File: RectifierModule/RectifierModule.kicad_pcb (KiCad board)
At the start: 2 copper layers, 45 x 70 mm, 26 parts, among them J201 RectifierIn, J202 Switch, J203 Digital VA measure, J204 VOut, J301 AC_IN, J302 Rectifier_out, J401 VA, J402 FAN, J403 Extra, Q201 BD139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

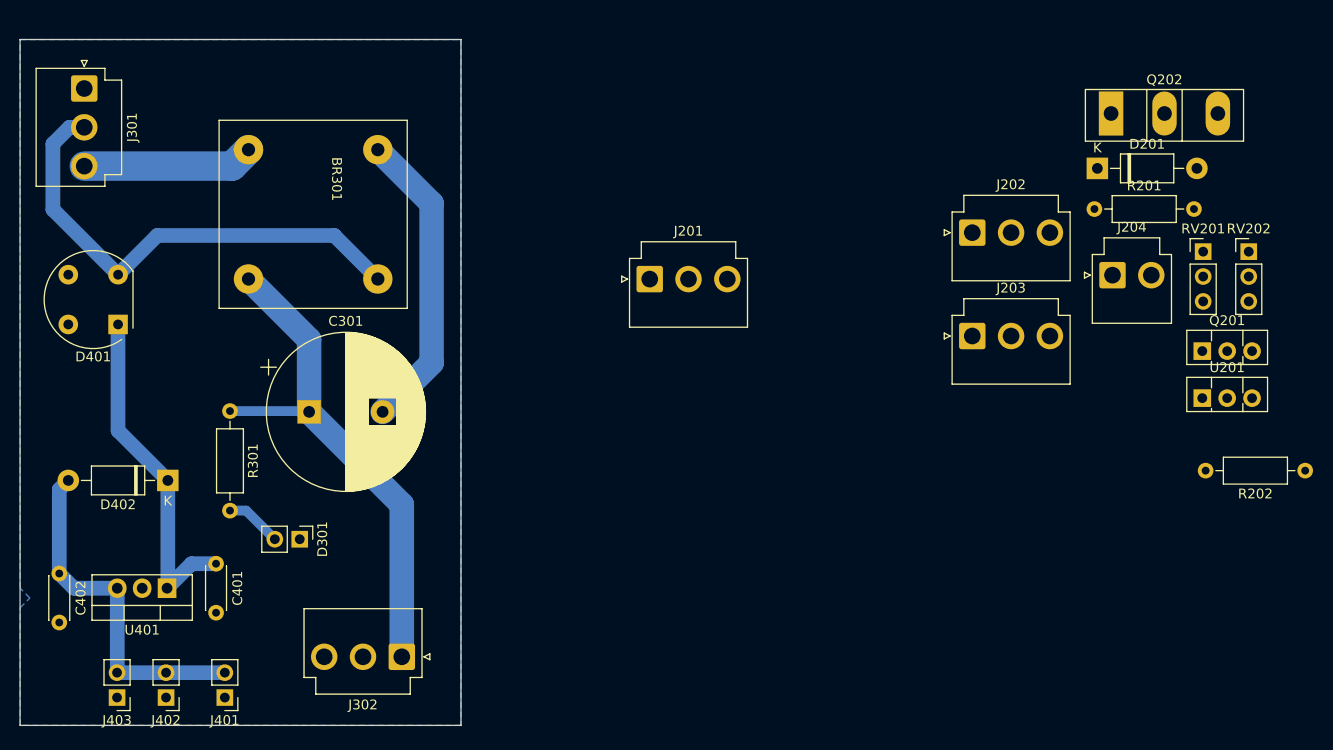
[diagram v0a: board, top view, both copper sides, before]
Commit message: Generated PCB layout
Some minor updates in the schematic and created the PCB layout for the rectifier module
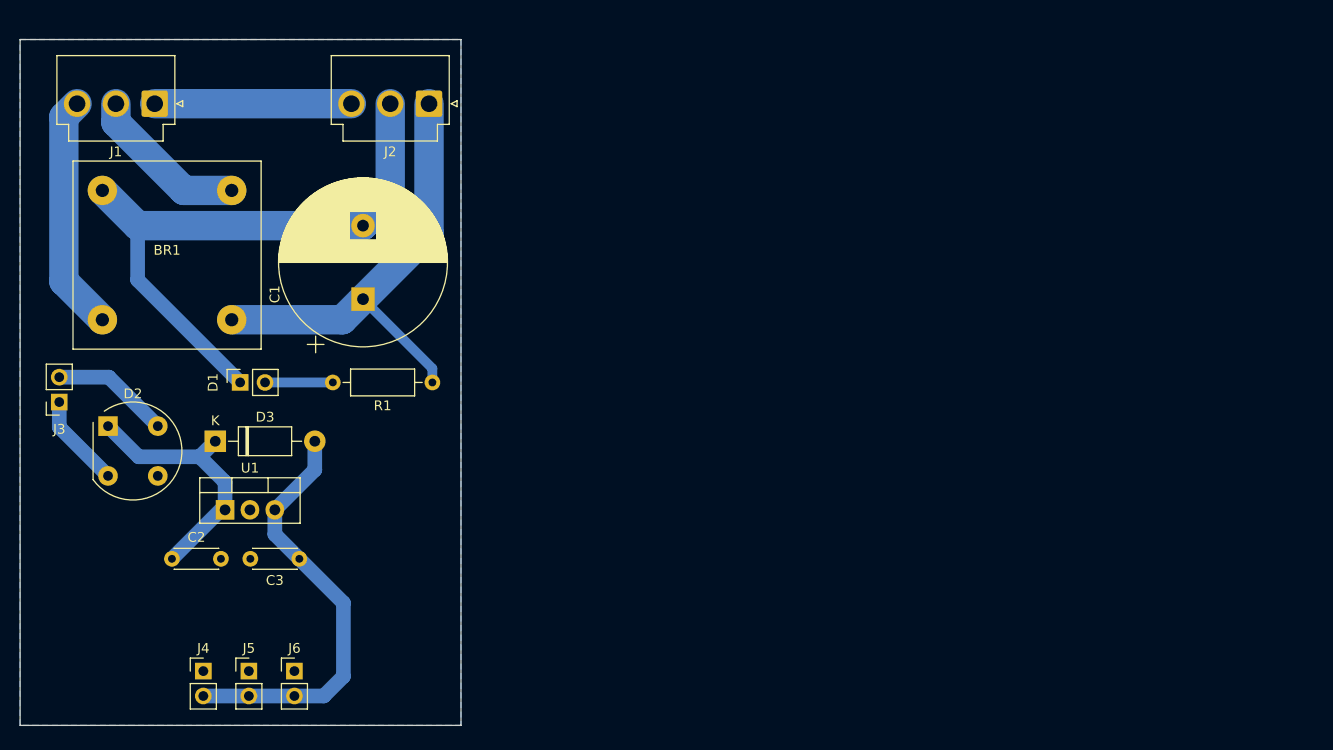
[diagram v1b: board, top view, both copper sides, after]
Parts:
- removed BR301: BRIDGE_RECTIFIER_CLASSIC, BridgeRectifiers:BR-10X
- removed C301: 4700u, Capacitor_THT:CP_Radial_D16.0mm_P7.50mm
- removed C401, C402: .1uF, Capacitor_THT:C_Disc_D4.3mm_W1.9mm_P5.00mm
- removed D201, D402: 1N4007, Diode_THT:D_DO-41_SOD81_P10.16mm_Horizontal
- removed D301: LED, Connector_PinHeader_2.54mm:PinHeader_1x02_P2.54mm_Vertical
- removed D401: W06G, Diode_THT:Diode_Bridge_Round_D9.8mm
- removed J201: RectifierIn, Connector_JST:JST_VH_B3P-VH-B_1x03_P3.96mm_Vertical
- removed J202: Switch, Connector_JST:JST_VH_B3P-VH-B_1x03_P3.96mm_Vertical
- removed J203: Digital VA measure, Connector_JST:JST_VH_B3P-VH_1x03_P3.96mm_Vertical
- removed J204: VOut, Connector_JST:JST_VH_B2P-VH_1x02_P3.96mm_Vertical
- removed J301: AC_IN, Connector_JST:JST_VH_B3P-VH-B_1x03_P3.96mm_Vertical
- removed J302: Rectifier_out, Connector_JST:JST_VH_B3P-VH-B_1x03_P3.96mm_Vertical
- removed J401: VA, Connector_PinHeader_2.54mm:PinHeader_1x02_P2.54mm_Vertical
- removed J402: FAN, Connector_PinHeader_2.54mm:PinHeader_1x02_P2.54mm_Vertical
- removed J403: Extra, Connector_PinHeader_2.54mm:PinHeader_1x02_P2.54mm_Vertical
- removed Q201: BD139, Package_TO_SOT_THT:TO-126-3_Vertical
- removed Q202: TIP2955G, Package_TO_SOT_THT:TO-247-3_Vertical
- removed R201, R202: 220, Resistor_THT:R_Axial_DIN0207_L6.3mm_D2.5mm_P10.16mm_Horizontal
- removed R301: 10k, Resistor_THT:R_Axial_DIN0207_L6.3mm_D2.5mm_P10.16mm_Horizontal
- removed RV201: 5k, Connector_PinHeader_2.54mm:PinHeader_1x03_P2.54mm_Vertical
- removed RV202: 10k, Connector_PinHeader_2.54mm:PinHeader_1x03_P2.54mm_Vertical
- removed U201: LM317, Package_TO_SOT_THT:TO-126-3_Vertical
- removed U401: LM7812_TO220, Package_TO_SOT_THT:TO-220-3_Vertical
- added BR1: BRIDGE_RECTIFIER_CLASSIC, BridgeRectifiers:BR-10X, F.Cu at (31.0, 36.0)
- added C1: 4700u, Capacitor_THT:CP_Radial_D17.0mm_P7.50mm, F.Cu at (51.0, 40.5)
- added C2: .1uF, Capacitor_THT:C_Disc_D4.3mm_W1.9mm_P5.00mm, F.Cu at (31.5, 67.0)
- added C3: .1uF, Capacitor_THT:C_Disc_D4.3mm_W1.9mm_P5.00mm, F.Cu at (44.5, 67.0)
- added D1: LED, Connector_PinSocket_2.54mm:PinSocket_1x02_P2.54mm_Vertical, F.Cu at (38.5, 49.0)
- added D2: W06G, Diode_THT:Diode_Bridge_Round_D9.8mm, F.Cu at (25.0, 53.5)
- added D3: 1N4007, Diode_THT:D_DO-41_SOD81_P10.16mm_Horizontal, F.Cu at (35.9, 55.0)
- added J1: TransformerIn, Connector_JST:JST_VH_B3P-VH-B_1x03_P3.96mm_Vertical, F.Cu at (29.7, 20.6)
- added J2: Rectified Out, Connector_JST:JST_VH_B3P-VH-B_1x03_P3.96mm_Vertical, F.Cu at (57.7, 20.6)
- added J3: AuxIn, Connector_PinSocket_2.54mm:PinSocket_1x02_P2.54mm_Vertical, F.Cu at (20.0, 51.0)
- added J4: VA, Connector_PinHeader_2.54mm:PinHeader_1x02_P2.54mm_Vertical, F.Cu at (34.7, 78.5)
- added J5: FAN, Connector_PinHeader_2.54mm:PinHeader_1x02_P2.54mm_Vertical, F.Cu at (39.4, 78.5)
- added J6: Extra, Connector_PinHeader_2.54mm:PinHeader_1x02_P2.54mm_Vertical, F.Cu at (44.0, 78.5)
- added R1: 220, Resistor_THT:R_Axial_DIN0207_L6.3mm_D2.5mm_P10.16mm_Horizontal, F.Cu at (58.1, 49.0)
- added U1: LM7812_TO220, Package_TO_SOT_THT:TO-220-3_Vertical, F.Cu at (36.9, 62.0)
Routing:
- net /30V-: track 0.00 -> 62.0 mm
- net /LM317_Module/RectifiedOut+: track 53.2 -> 0.00 mm
- net /Auxilliaries/Aux_input_N: track 50.0 -> 0.00 mm
- net /30V+: track 0.00 -> 48.4 mm
- net /Aux_out: track 0.00 -> 43.7 mm
- net /Auxilliaries/Aux_out: track 36.1 -> 0.00 mm
- net /Auxilliaries/RectifiedOut+: track 35.1 -> 0.00 mm
- net /LM317_Module/RectifiedOut-: track 31.1 -> 0.00 mm
- net /12V+: track 0.00 -> 26.9 mm
- net /AC_IN_L: track 0.00 -> 24.2 mm
- net /CentreTap: track 0.00 -> 20.1 mm
- net /Rectifier Module/AC_L: track 17.5 -> 0.00 mm
- net /AC_IN_N: track 0.00 -> 16.6 mm
- net /Aux_input_L: track 0.00 -> 12.1 mm
- net /Aux_input_N: track 0.00 -> 9.60 mm
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
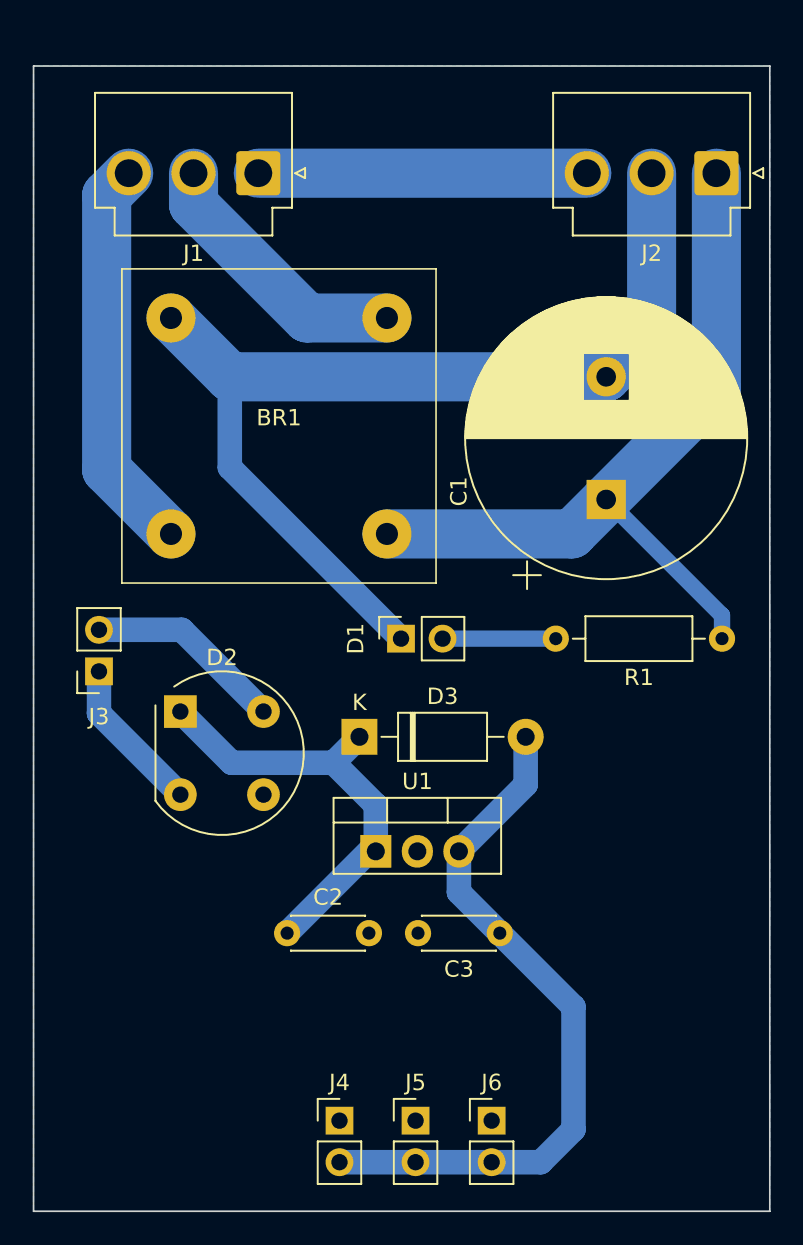
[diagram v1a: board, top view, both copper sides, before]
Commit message: Updated the capacitor at input of 7812
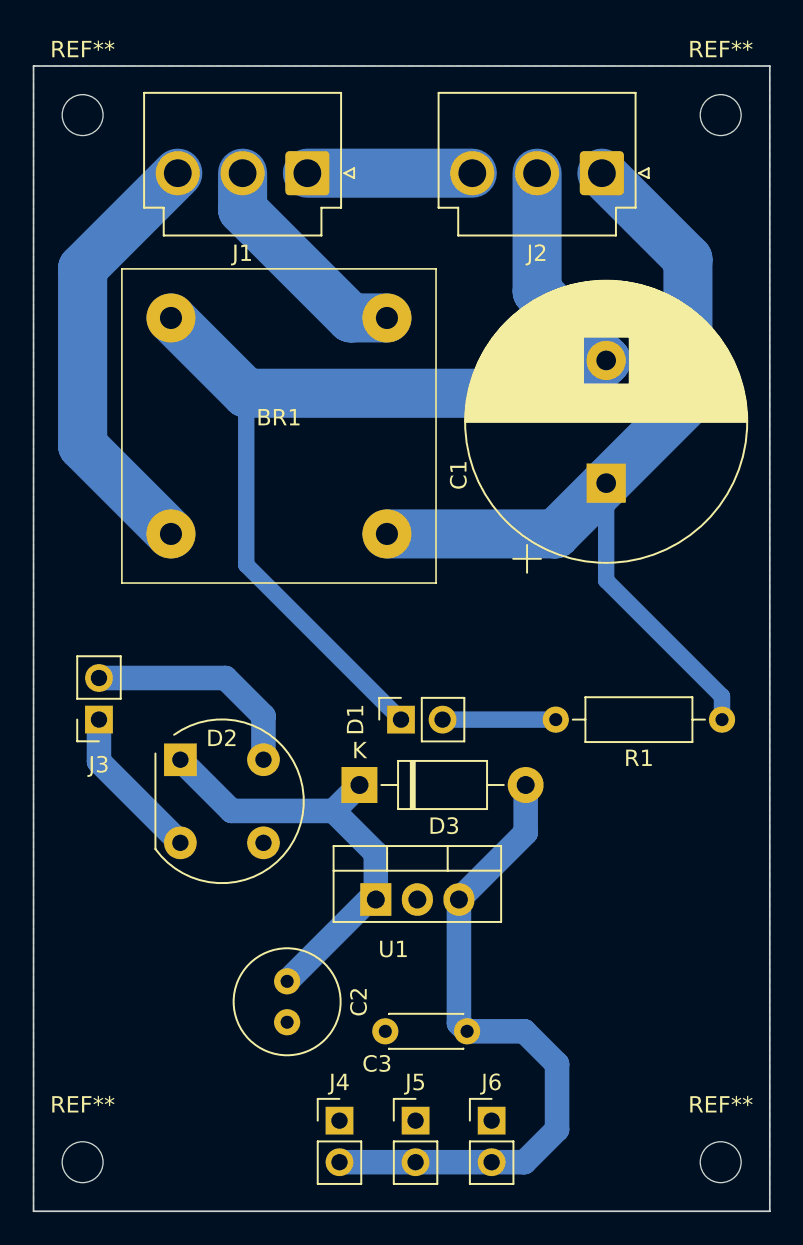
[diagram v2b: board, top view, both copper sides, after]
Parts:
- added REF**: MountingHole_2.5mm, MountingHole:MountingHole_2.5mm, F.Cu at (58.0, 81.0)
- added REF**: MountingHole_2.5mm, MountingHole:MountingHole_2.5mm, F.Cu at (58.0, 17.0)
- added REF**: MountingHole_2.5mm, MountingHole:MountingHole_2.5mm, F.Cu at (19.0, 81.0)
- added REF**: MountingHole_2.5mm, MountingHole:MountingHole_2.5mm, F.Cu at (19.0, 17.0)
- C2: value .1uF -> 100u; footprint Capacitor_THT:C_Disc_D4.3mm_W1.9mm_P5.00mm -> Capacitor_THT:C_Radial_D6.3mm_H11.0mm_P2.50mm
- moved J2 7.00 mm to (50.7, 20.6)
- moved C3 6.32 mm to (42.5, 73.0)
- moved D1 4.95 mm to (38.5, 53.9)
- moved R1 4.95 mm to (58.1, 53.9)
- moved J1 3.00 mm to (32.7, 20.6)
- moved D2 2.95 mm to (25.0, 56.4)
- moved D3 2.95 mm to (35.9, 57.9)
- moved J3 2.95 mm to (20.0, 53.9)
- moved C2 2.94 mm to (31.5, 69.9), turned to -90 degrees
- moved U1 2.94 mm to (36.9, 64.9)
- moved C1 1.00 mm to (51.0, 39.5)
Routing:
- net /CentreTap: track 20.1 -> 10.1 mm
- net /30V+: track 48.4 -> 55.4 mm
- net /30V-: track 62.0 -> 66.4 mm
- net /AC_IN_N: track 16.6 -> 13.8 mm
- net /AC_IN_L: track 24.2 -> 26.7 mm
- net /Aux_out: track 43.7 -> 41.4 mm
- net /Aux_input_L: track 12.1 -> 13.7 mm

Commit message: Add mounting holes and their footprints
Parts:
- removed REF** (x4): MountingHole_2.5mm, MountingHole:MountingHole_2.5mm
- added H1: MountingHole, MountingHole:MountingHole_2.5mm, F.Cu at (19.0, 81.0)
- added H2: MountingHole, MountingHole:MountingHole_2.5mm, F.Cu at (58.0, 81.0)
- added H3: MountingHole, MountingHole:MountingHole_2.5mm, F.Cu at (58.0, 17.0)
- added H4: MountingHole, MountingHole:MountingHole_2.5mm, F.Cu at (19.0, 17.0)
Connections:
- J1 pad 1: /CentreTap -> /AC_IN_N
- J1 pad 2: /AC_IN_N -> /CentreTap
- J2 pad 2: /30V- -> /CentreTap
- J2 pad 3: /CentreTap -> /30V-
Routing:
- net /CentreTap: track 10.1 -> 23.1 mm
- net /30V-: track 66.4 -> 68.0 mm
- net /AC_IN_N: track 13.8 -> 12.2 mm

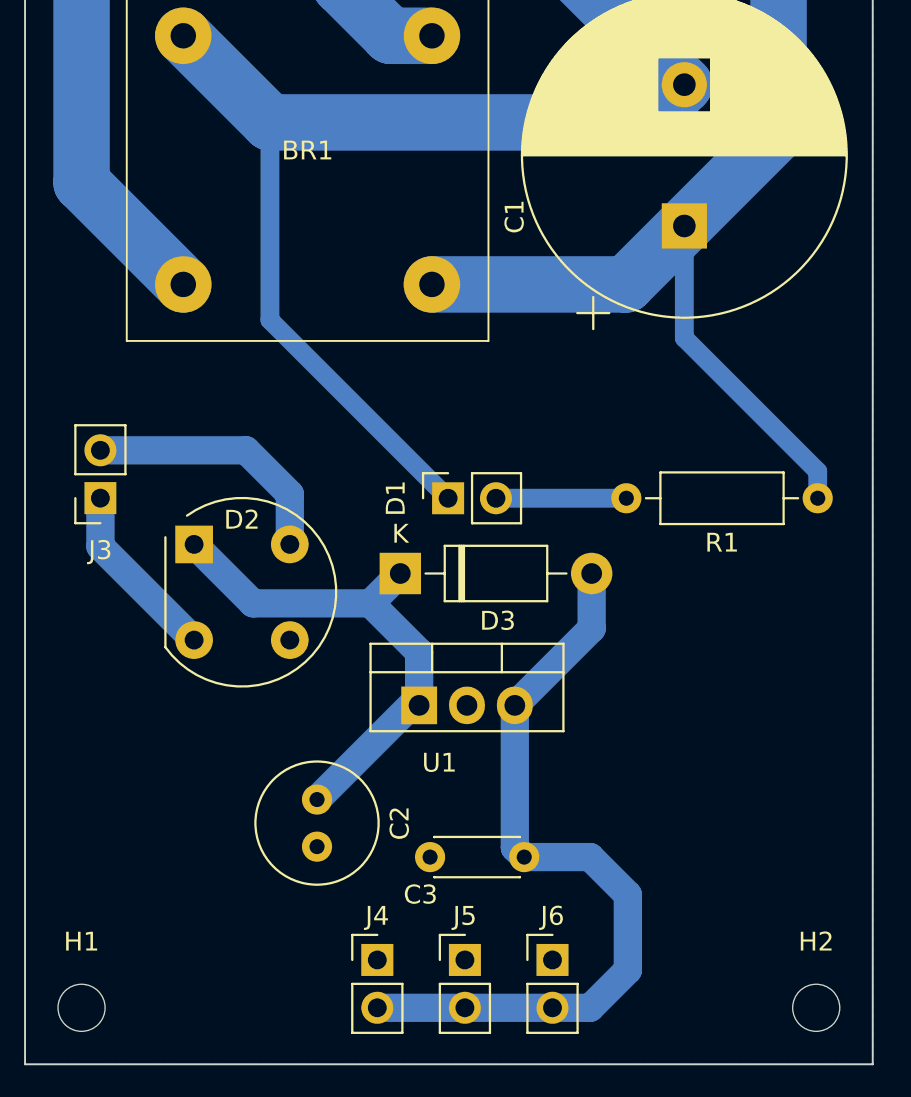
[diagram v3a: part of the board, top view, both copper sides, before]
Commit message: Added heat sink and made changes to accommodate the heatsink
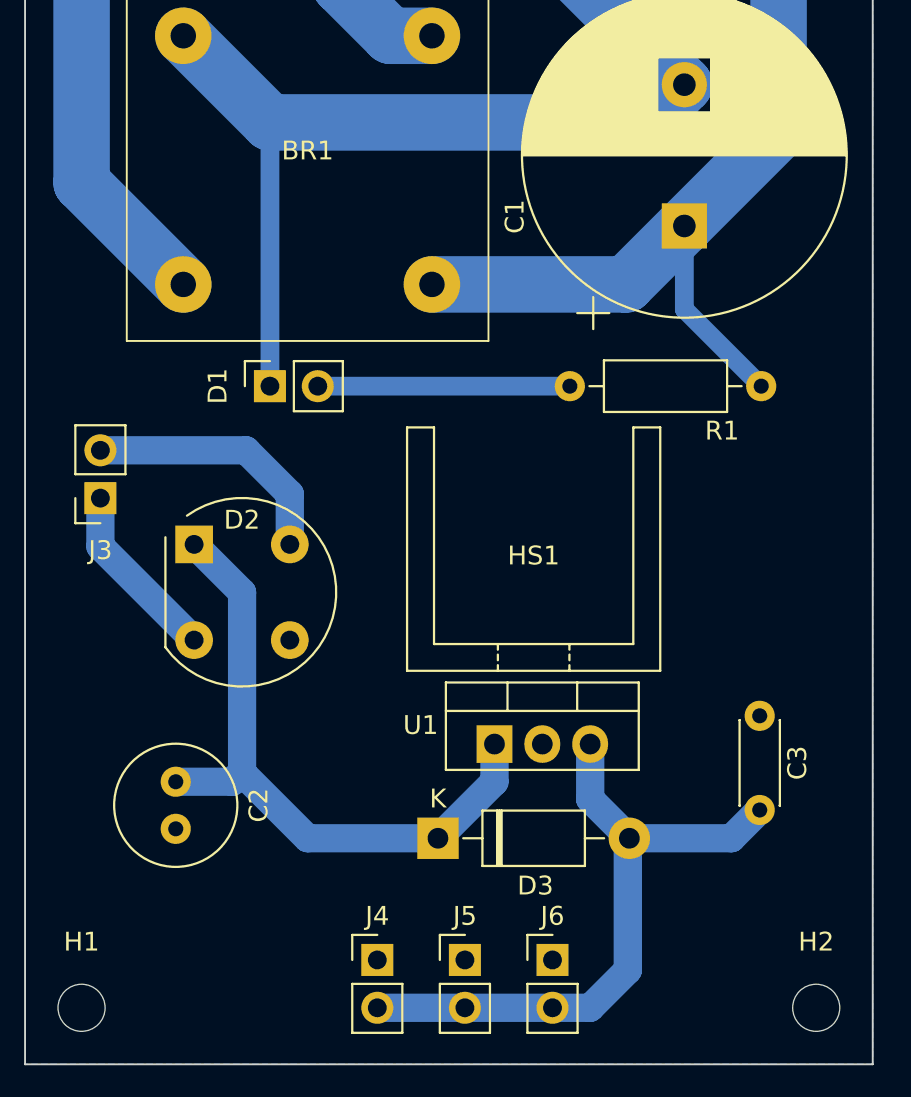
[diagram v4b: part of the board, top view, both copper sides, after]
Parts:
- added HS1: Heatsink, Heatsink:Heatsink_Stonecold_HS-S03_13.21x12.7mm, F.Cu at (43.0, 63.0)
- moved D3 14.2 mm to (37.9, 72.0)
- moved C3 12.7 mm to (55.0, 70.5), turned to 90 degrees
- moved D1 11.2 mm to (29.0, 48.0)
- moved C2 7.56 mm to (24.0, 69.0)
- moved R1 6.66 mm to (55.1, 48.0)
- moved U1 4.50 mm to (40.9, 67.0)
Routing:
- net /30V-: track 68.0 -> 58.2 mm
- net /12V+: track 26.9 -> 35.0 mm
- net /30V+: track 55.4 -> 48.2 mm
- net /Aux_out: track 41.4 -> 34.6 mm
- net Net-(D1-A): track 6.92 -> 13.4 mm
